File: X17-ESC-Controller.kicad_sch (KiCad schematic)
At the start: 8 parts, among them IC1 STM32F091CCT7, J2 DF11-10DP-2DSA24, J3 DF11-10DP-2DSA24, U1 AZ1117H-ADJ, U2 MAX485CSA+T

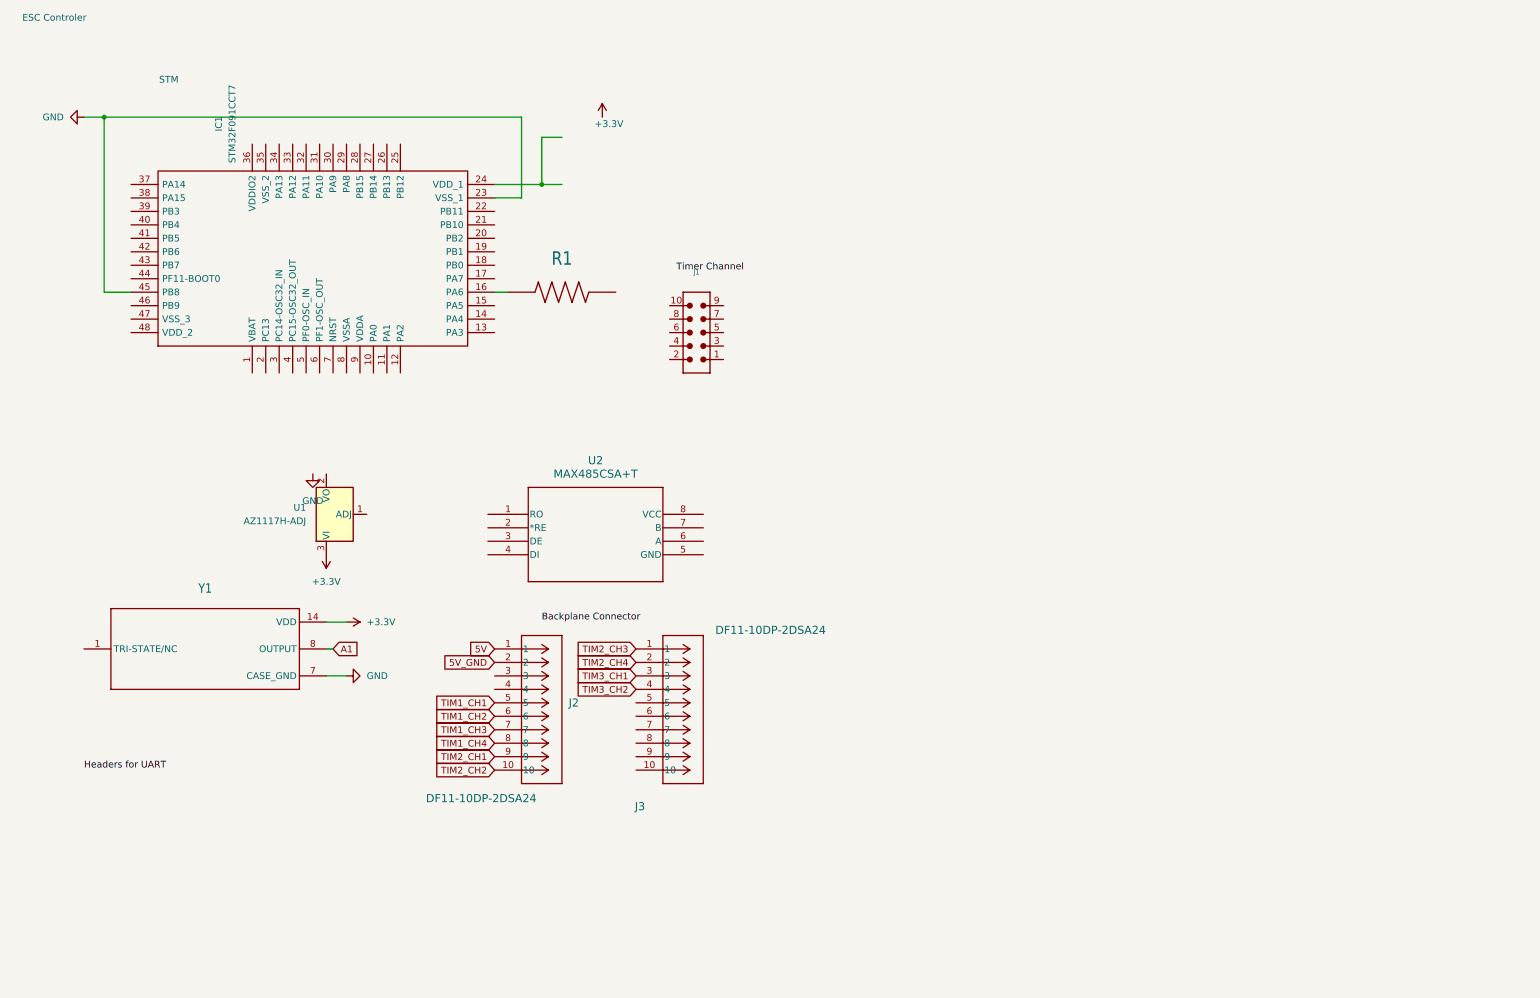
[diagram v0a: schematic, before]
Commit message: X17 ESC-Controller
ESC-Controller Schematic for Alumni Design Review
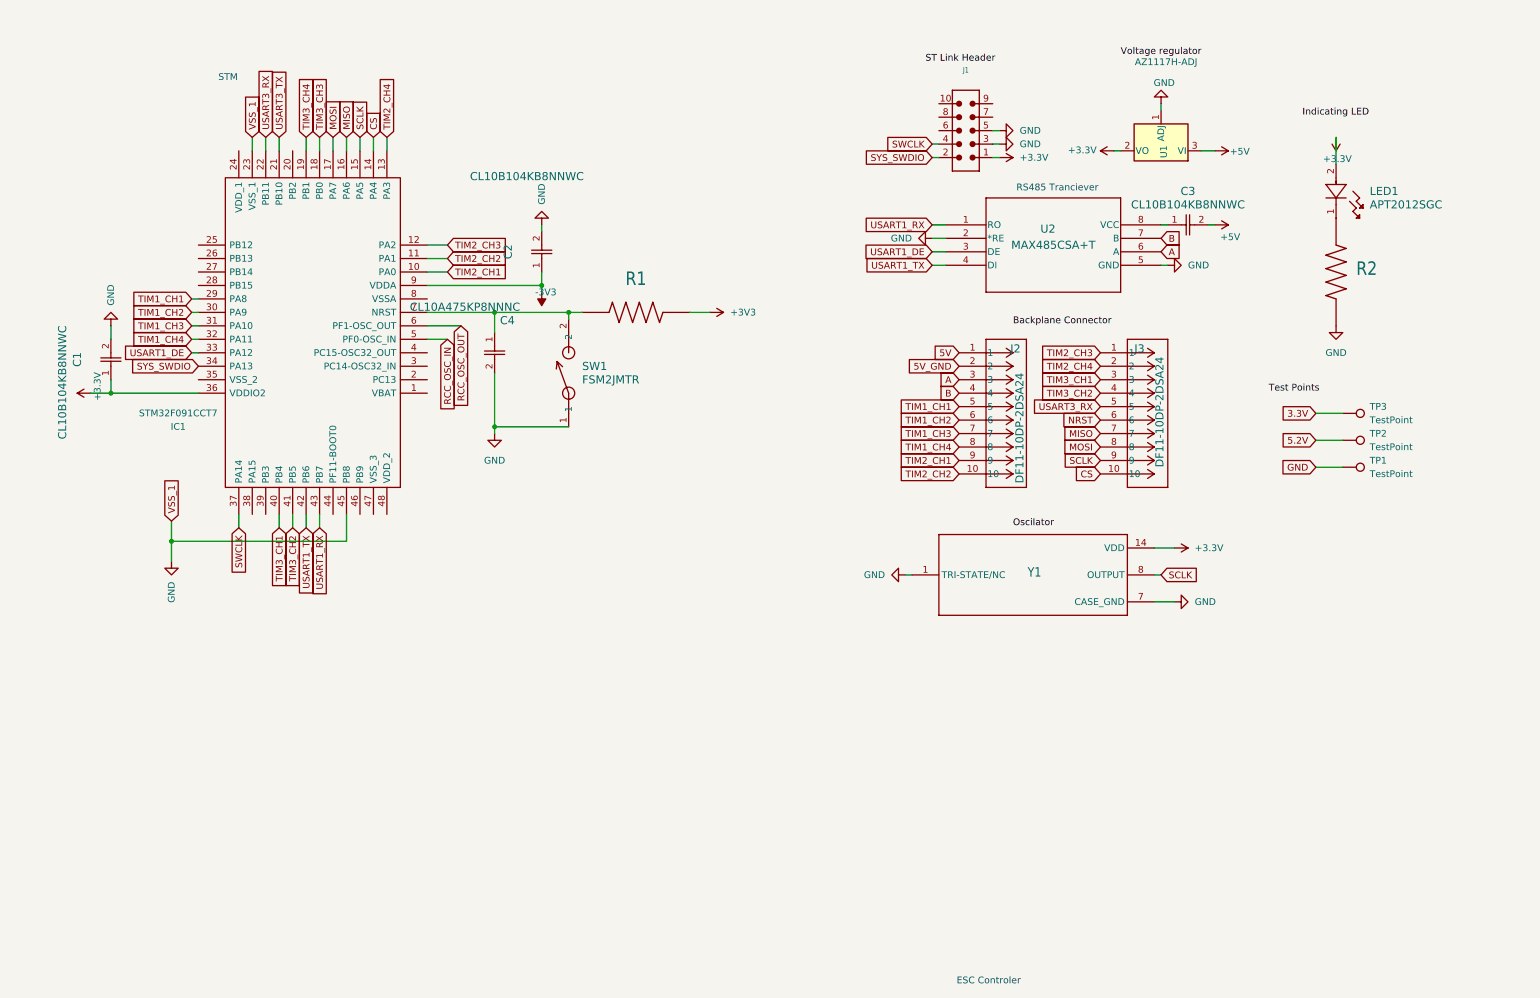
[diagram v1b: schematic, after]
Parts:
- removed R1: ~, CRGCQ0603F1K0:RESC1608X55N, symbol CRGCQ0603F1K0:CRGCQ0603F1K0
- added C1, C2, C3: CL10B104KB8NNWC, CAP_CL10_SAM, symbol 2024-10-16_23-50-01:CL10B104KB8NNWC
- added C4: CL10A475KP8NNNC, CAP_0603_CL10A_1P6XP8_SAM, symbol 2024-10-19_19-16-32:CL10A475KP8NNNC
- added LED1: APT2012SGC, LED_APT2012SGC_KNB, symbol 2024-10-19_19-01-08:APT2012SGC
- added R1, R2: ~, CRGCQ0603J150R:RESC1608X55N, symbol CRGCQ0603J150R:CRGCQ0603J150R
- added SW1: FSM2JMTR, SW_FSM2JMTR_TEC, symbol 2024-10-19_19-07-35:FSM2JMTR
- added TP1, TP2, TP3: TestPoint, symbol Connector:TestPoint
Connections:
- net A1 is gone; now on net SCLK: Y1.8 (OUTPUT)
- net +3.3V: now also IC1.36 (VDDIO2), J1.1, U1.2 (VO), C1.1, LED1.2; no longer U1.3 (VI)
- net GND: now also J1.3, J1.5, U1.1 (ADJ), U2.2 (*RE), U2.5 (GND), Y1.1 (TRI-STATE/NC), C1.2, C2.2, C4.2, R2.1, SW1.1, TP1.1
- net TIM1_CH1: now also IC1.29 (PA8)
- net TIM1_CH2: now also IC1.30 (PA9)
- net TIM1_CH3: now also IC1.31 (PA10)
- net TIM1_CH4: now also IC1.32 (PA11)
- net TIM2_CH1: now also IC1.10 (PA0)
- net TIM2_CH2: now also IC1.11 (PA1)
- net TIM2_CH3: now also IC1.12 (PA2)
- net TIM2_CH4: now also IC1.13 (PA3)
- net TIM3_CH1: now also IC1.40 (PB4)
- net TIM3_CH2: now also IC1.41 (PB5)
- net MISO: now reaches IC1.16 (PA6)
- net MISO: now also J3.7
- net A: now reaches J2.3
- net A: now also U2.6 (A)
- net B: now reaches J2.4
- net B: now also U2.7 (B)
- net USART1_RX: now reaches U2.1 (RO)
- net USART1_RX: now also IC1.43 (PB7)
- net USART1_DE: now reaches U2.3 (DE)
- net USART1_DE: now also IC1.33 (PA12)
- net USART1_TX: now reaches U2.4 (DI)
- net USART1_TX: now also IC1.42 (PB6)
- net at U2.8 (VCC): now also C3.1
- net CS: now reaches IC1.14 (PA4)
- net CS: now also J3.10
- net SCLK: now reaches IC1.15 (PA5)
- net SCLK: now also J3.9
- net MOSI: now reaches IC1.17 (PA7)
- net MOSI: now also J3.8
- net TIM3_CH3: now reaches IC1.18 (PB0)
- net TIM3_CH4: now reaches IC1.19 (PB1)
- net USART3_TX: now reaches IC1.21 (PB10)
- net USART3_RX: now reaches IC1.22 (PB11)
- net USART3_RX: now also J3.5
- net SYS_SWDIO: now reaches IC1.34 (PA13)
- net SYS_SWDIO: now also J1.2
- net SWCLK: now reaches IC1.37 (PA14)
- net SWCLK: now also J1.4
- net RCC_OSC_IN: now reaches IC1.5 (PF0-OSC_IN)
- net RCC_OSC_OUT: now reaches IC1.6 (PF1-OSC_OUT)
- net at IC1.7 (NRST): now also C4.1, R1.1, SW1.2
- net -3V3: now reaches IC1.9 (VDDA)
- net -3V3: now also C2.1
- net NRST: now reaches J3.6
- new net: LED1.1, R2.2
- new net +3V3: R1.2
- new net +5V: C3.2, U1.3 (VI)
- new net 3.3V: TP3.1
- new net 5.2V: TP2.1
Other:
- note added: "RS485 Tranciever"
- moved on the sheet: IC1, J1, J2, J3, U1, U2, Y1

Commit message: Add files via upload
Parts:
- removed C1, C2: CL10B104KB8NNWC, CAP_CL10_SAM, symbol 2024-10-16_23-50-01:CL10B104KB8NNWC
- removed C4: CL10A475KP8NNNC, CAP_0603_CL10A_1P6XP8_SAM, symbol 2024-10-19_19-16-32:CL10A475KP8NNNC
- removed R1, R2: ~, CRGCQ0603J150R:RESC1608X55N, symbol CRGCQ0603J150R:CRGCQ0603J150R
- removed SW1: FSM2JMTR, SW_FSM2JMTR_TEC, symbol 2024-10-19_19-07-35:FSM2JMTR
- removed U1: AZ1117H-ADJ, Package_TO_SOT_SMD:SOT-223-3_TabPin2, symbol Regulator_Linear:AZ1117H-ADJ
- removed Y1: ~, ACO-8.000MHZ-EK:XTAL_ACO-8.000MHZ-EK, symbol ACO-8.000MHZ-EK:ACO-8.000MHZ-EK
- added C1, C2: 18pF, symbol Device:C
- added C5, C6: GRM188R60G226MEA0D, G-188_MUR, symbol 2024-10-30_23-26-29:GRM188R60G226MEA0D
- added R1: 20k, symbol Device:R_US
- added R2: 4.2k, symbol Device:R_US
- added U3: ~, X16-ESC-Controller:SOT223_AZ1117I_6P5X3P5_DIO, symbol X16-ESC-Controller:AZ1117IH-3.3TRG1
- added Y2: Crystal, symbol Device:Crystal
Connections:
- net -3V3 is gone; now on net +3.3V: IC1.9 (VDDA)
- net +3.3V: now also IC1.24 (VDD_1); no longer LED1.2
- net +5V: now also C5.2, U3.3 (INPUT)
- net B: now also R1.1
- net GND: now also IC1.44 (PF11-BOOT0), LED1.1, C1.2, C2.2, C5.1, C6.2, R1.2, U3.1 (ADJ/GND); no longer U2.2 (*RE)
- net NRST: now also IC1.7 (NRST)
- net RCC_OSC_IN: now also C2.1, Y2.1
- net RCC_OSC_OUT: now also C1.1, Y2.2
- net USART1_DE: now also U2.2 (*RE)
- net NC: now reaches IC1.1 (VBAT)
- net NC: now also IC1.2 (PC13), IC1.20 (PB2), IC1.25 (PB12), IC1.26 (PB13), IC1.27 (PB14), IC1.3 (PC14-OSC32_IN), IC1.35 (VSS_2), IC1.38 (PA15), IC1.39 (PB3), IC1.4 (PC15-OSC32_OUT), IC1.46 (PB9), IC1.47 (VSS_3), IC1.48 (VDD_2), IC1.8 (VSSA), J1.10, J1.6, J1.7, J1.8, J1.9
- net LED: now reaches IC1.28 (PB15)
- net LED: now also R2.1
- new net: LED1.2, R2.2
- new net -3.3V: C6.1, U3.2 (OUTPUT), U3.4 (OUTPUT)
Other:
- moved on the sheet: C3, J1, J2, J3, LED1, U2

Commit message: layout fix
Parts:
- removed C3: CL10B104KB8NNWC, CAP_CL10_SAM, symbol 2024-10-16_23-50-01:CL10B104KB8NNWC
- removed C5, C6: GRM188R60G226MEA0D, G-188_MUR, symbol 2024-10-30_23-26-29:GRM188R60G226MEA0D
- removed IC1: STM32F091CCT7, QFP50P900X900X160-48N, symbol STM32F091CCT7:STM32F091CCT7
- removed J1: ~, Eagle_WR-BHD_rev22c:61201021621, symbol Eagle_WR-BHD_rev22c:6120XX21621_61201021621
- removed J2, J3: DF11-10DP-2DSA24, CON10_2X5_UF_DF11_HIR, symbol 2024-10-12_13-00-01:DF11-10DP-2DSA24
- removed LED1: APT2012SGC, LED_APT2012SGC_KNB, symbol 2024-10-19_19-01-08:APT2012SGC
- removed U2: MAX485CSA+T, 21-0041-3-M_90-0096-8L_MXM, symbol 2024-10-12_15-43-15:MAX485CSA+T
- removed U3: ~, X16-ESC-Controller:SOT223_AZ1117I_6P5X3P5_DIO, symbol X16-ESC-Controller:AZ1117IH-3.3TRG1
- removed Y2: Crystal, symbol Device:Crystal
- added C10, C9: 4.7u, Capacitor_SMD:C_0603_1608Metric_Pad1.08x0.95mm_HandSolder, symbol Device:C
- added C11, C3, C4, C5, C7, C8: 0.1u, Capacitor_SMD:C_0603_1608Metric_Pad1.08x0.95mm_HandSolder, symbol Device:C
- added C12: 10u, Capacitor_SMD:C_0603_1608Metric_Pad1.08x0.95mm_HandSolder, symbol Device:C
- added C13: 22u, Capacitor_SMD:C_0603_1608Metric_Pad1.08x0.95mm_HandSolder, symbol Device:C
- added C6: 1u, Capacitor_SMD:C_0603_1608Metric_Pad1.08x0.95mm_HandSolder, symbol Device:C
- added D1, D2, D3: D, LED_SMD:LED_0805_2012Metric_Pad1.15x1.40mm_HandSolder, symbol Device:D
- added J1: ~, Backplane Connector:CON10_2X5_UF_DF11_HIR, symbol Backplane Connector:DF11-10DS-2DSA05
- added J10, J11, J3, J8, J9: Conn_01x02, Connector_PinHeader_2.54mm:PinHeader_1x02_P2.54mm_Vertical, symbol Connector_Generic:Conn_01x02
- added J4: Conn_02x05_Odd_Even, Connector_IDC:IDC-Header_2x05_P2.54mm_Vertical, symbol Connector_Generic:Conn_02x05_Odd_Even
- added J5, J6: Conn_01x04, Connector_PinHeader_2.54mm:PinHeader_1x04_P2.54mm_Vertical, symbol Connector_Generic:Conn_01x04
- added J7: Conn_01x03, Connector_PinHeader_2.54mm:PinHeader_1x03_P2.54mm_Vertical, symbol Connector_Generic:Conn_01x03
- added R3: 120, Resistor_SMD:R_0603_1608Metric_Pad0.98x0.95mm_HandSolder, symbol Device:R_US
- added R4, R5: 10k, Resistor_SMD:R_0603_1608Metric_Pad0.98x0.95mm_HandSolder, symbol Device:R_US
- added R6: 100, Resistor_SMD:R_0603_1608Metric_Pad0.98x0.95mm_HandSolder, symbol Device:R_US
- added R7: 240, Resistor_SMD:R_0603_1608Metric_Pad0.98x0.95mm_HandSolder, symbol Device:R_US
- added SW1: SW_Push, Button-SW_FSM2JMTR_TEC:SW_FSM2JMTR_TEC, symbol Switch:SW_Push
- added U2: AZ1117-3.3, Package_TO_SOT_SMD:SOT-223-3_TabPin2, symbol Regulator_Linear:AZ1117-3.3
- added U3: MAX7375AXR805, Package_TO_SOT_SMD:SOT-323_SC-70_Handsoldering, symbol Oscillator:MAX7375AXR805
- added U4: STM32F091CCTx, Package_QFP:LQFP-48_7x7mm_P0.5mm, symbol MCU_ST_STM32F0:STM32F091CCTx
- added U5: MAX485, MAX485:SO08, symbol MAX485:MAX485
- C1: value 18pF -> 10n; footprint (none) -> Capacitor_SMD:C_0603_1608Metric_Pad1.08x0.95mm_HandSolder
- C2: value 18pF -> 0.1u; footprint (none) -> Capacitor_SMD:C_0603_1608Metric_Pad1.08x0.95mm_HandSolder
- R1: value 20k -> 10k; footprint (none) -> Resistor_SMD:R_0603_1608Metric_Pad0.98x0.95mm_HandSolder
- R2: value 4.2k -> 100; footprint (none) -> Resistor_SMD:R_0603_1608Metric_Pad0.98x0.95mm_HandSolder
- TP1, TP2, TP3: footprint (none) -> TestPoint:TestPoint_Pad_D4.0mm
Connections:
- net 3.3V is gone; now on net +3.3V: TP3.1
- net 5.2V is gone; now on net +5V: TP2.1
- net RCC_OSC_OUT is gone; now on net +3.3V: C1.1
- net +3.3V: now also C2.1, R2.2, C10.1, C13.1, C4.1, C5.1, C6.1, C7.1, C8.1, C9.1, J4.7 (Pin_7), J4.8 (Pin_8), R5.2, U2.2 (VO), U3.1 (V+), U4.1 (VBAT), U4.24 (VDD), U4.36 (VDDIO2), U4.48 (VDD), U4.9 (VDDA)
- net +5V: now also R1.2, C11.1, C12.1, J1.1, R7.2, U2.3 (VI), U5.8 (VCC)
- net A: now also R1.1, J1.17, J1.4, J8.2 (Pin_2), R3.2, U5.6 (A)
- net B: now also J1.18, J1.6, J8.1 (Pin_1), R3.1, R4.2, U5.7 (B); no longer R1.1
- net CS: now also J5.4 (Pin_4), U4.38 (PA15)
- net GND: now also C10.2, C11.2, C12.2, C13.2, C3.2, C4.2, C5.2, C6.2, C7.2, C8.2, C9.2, D1.1 (K), D2.1 (K), D3.1 (K), J1.2, J4.3 (Pin_3), J4.4 (Pin_4), R4.1, SW1.1, U2.1 (GND), U3.3 (GND), U4.23 (VSS), U4.35 (VSS), U4.44 (PF11), U4.47 (VSS), U4.8 (VSSA), U5.5 (GND); no longer R1.2
- net MISO: now also J5.2 (Pin_2), U4.40 (PB4)
- net MOSI: now also J5.1 (Pin_1), U4.41 (PB5)
- net NRST: now also C3.1, J1.16, J4.1 (Pin_1), R5.1, SW1.2, U4.7 (NRST)
- net RCC_OSC_IN: now also U3.2 (CLOCK), U4.5 (PF0); no longer C2.1
- net SCLK: now also J5.3 (Pin_3), U4.39 (PB3)
- net SWCLK: now also J4.6 (Pin_6), U4.37 (PA14)
- net SYS_SWDIO: now also J4.2 (Pin_2), U4.34 (PA13)
- net TIM1_CH1: now also J1.5, J6.1 (Pin_1), U4.29 (PA8)
- net TIM1_CH2: now also J1.3, J6.2 (Pin_2), U4.30 (PA9)
- net TIM1_CH3: now also J1.7, J6.3 (Pin_3), U4.31 (PA10)
- net TIM1_CH4: now also J1.8, J6.4 (Pin_4), U4.32 (PA11)
- net TIM2_CH1: now also J1.9, J10.1 (Pin_1), U4.10 (PA0)
- net TIM2_CH2: now also J1.10, J10.2 (Pin_2), U4.11 (PA1)
- net TIM2_CH3: now also J1.11, J11.1 (Pin_1), U4.12 (PA2)
- net TIM2_CH4: now also J1.12, J11.2 (Pin_2), U4.13 (PA3)
- net TIM3_CH1: now also J1.13, J3.1 (Pin_1), U4.16 (PA6)
- net TIM3_CH2: now also J1.14, J3.2 (Pin_2), U4.17 (PA7)
- net USART1_RX: now also J1.15, J9.2 (Pin_2), U4.43 (PB7)
- net USART1_TX: now also J9.1 (Pin_1), U4.42 (PB6)
- net USART3_RX: now also J7.1 (Pin_1), U4.22 (PB11), U5.1 (RO)
- net USART3_TX: now also J7.2 (Pin_2), U4.21 (PB10), U5.4 (DI)
- net LED: no longer names the net of R2.1
- net LED: now also D2.2 (A)
- new net: D3.2 (A), R7.1
- new net: D1.2 (A), R6.1
- new net: R6.2, U4.28 (PB15)
- new net USART3_DE: J7.3 (Pin_3), U4.19 (PB1), U5.2 (RE), U5.3 (DE)
- no-connect marks 0 -> 18
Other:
- note added: "1x 10n for VDDA 1x 1u for VDDA Pin 9"
- note added: "2x 100n for 2x VDD 1x 4.7u for 2x VDD 1x 100n for VDDIO2 1x 4.7u for VDDIO2 1x 100n for VBAT"
- note added: "5V to 3.3V Conversion"
- note added: "Oscillator"
- note added: "Programming Header"
- note added: "STM32"
- note added: "STM32 Decoupling Capacitors"
- note removed: "STM"
